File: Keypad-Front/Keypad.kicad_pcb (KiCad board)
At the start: 4 copper layers, 100.1 x 192.1 mm, 62 parts, among them J1 RTC STEMMA QT, J3 JST-PH 6, J4 JST-PH 6, J6 EXP QWIIC, J7 TOUCH QWIIC, U1 DS3231MZ, U2 LM1117-3.3, U3 CAP1214

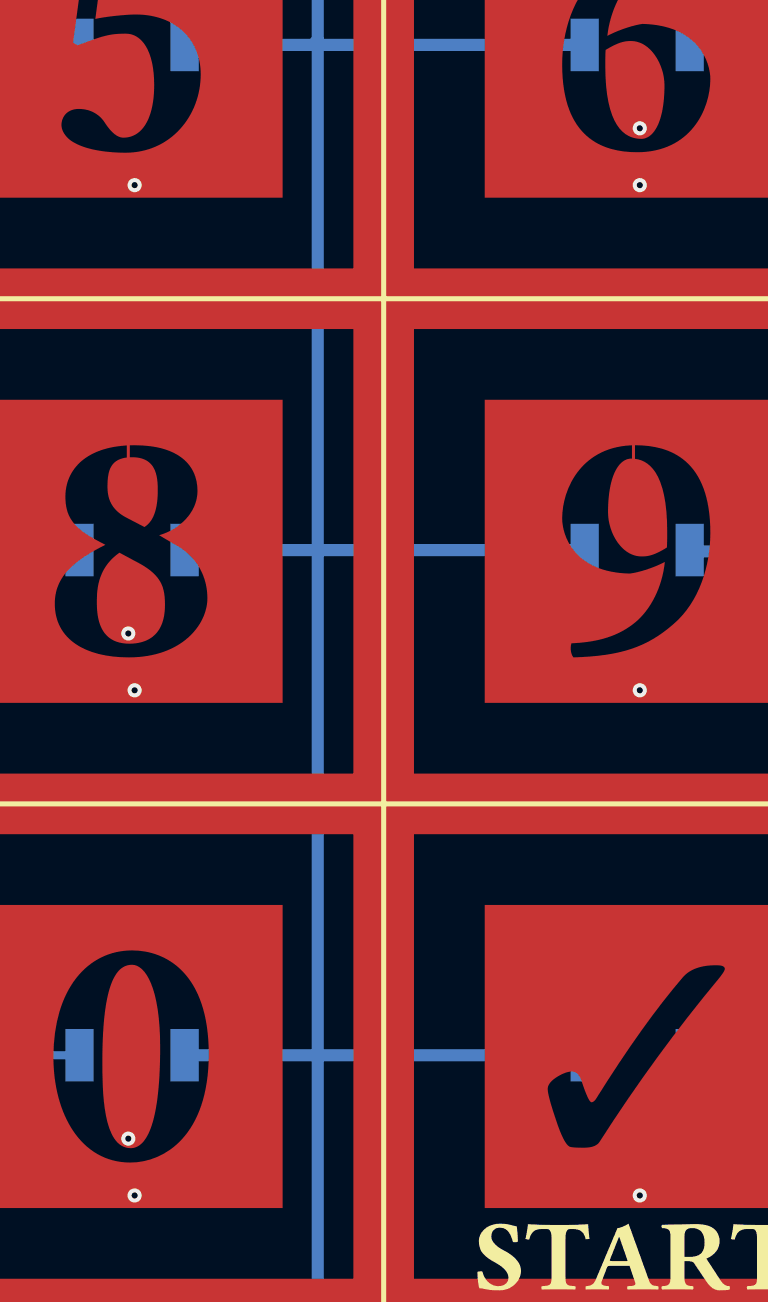
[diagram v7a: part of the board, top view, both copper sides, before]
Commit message: Third version, no vias to cast shadows.
Also add the BOM.
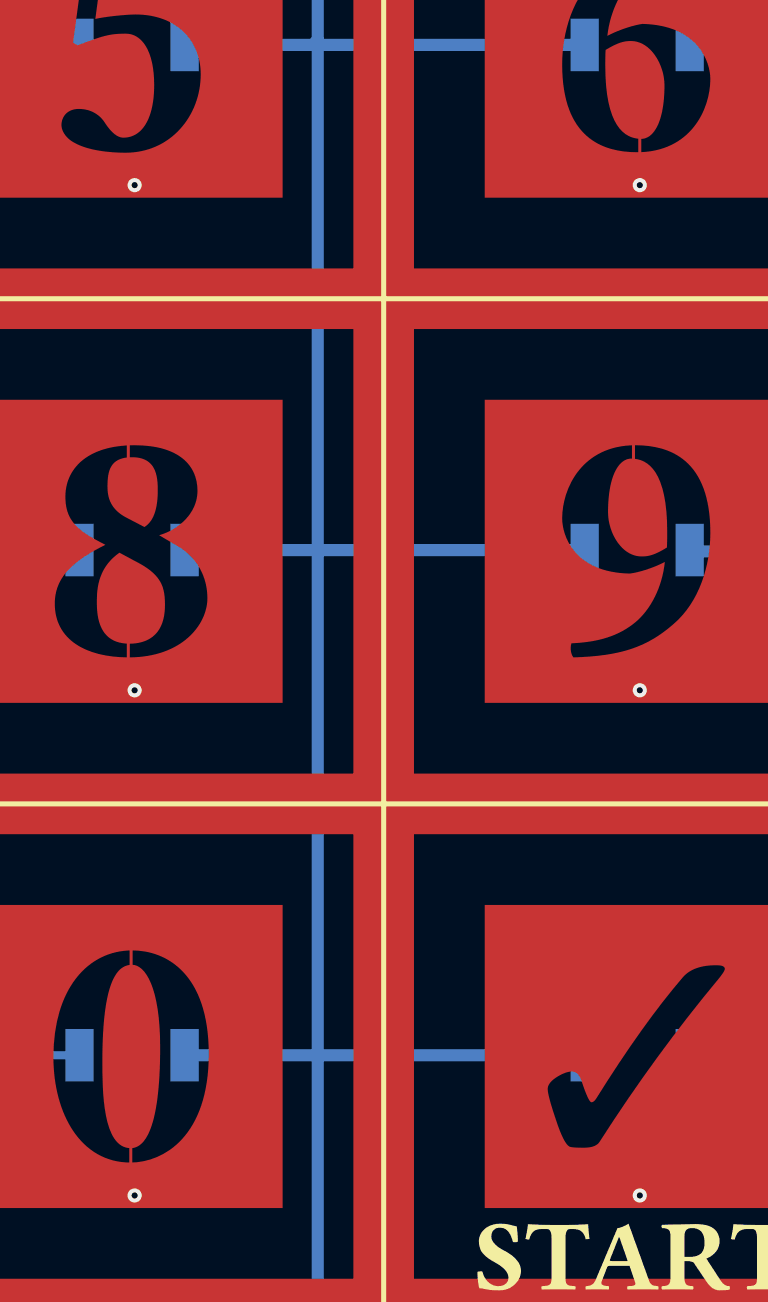
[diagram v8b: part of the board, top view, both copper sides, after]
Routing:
- net /TOUCH_11: track 22.0 -> 24.0 mm, vias 3 -> 2
- net /TOUCH_8: track 50.8 -> 50.4 mm, vias 3 -> 2
- net /TOUCH_6: vias 3 -> 2
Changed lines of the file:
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@@
   (segment (start 107.285311 184.267544) (end 106.5625 183.544733) (width 0.15) (layer "B.Cu") (net 48))
   (segment (start 106.5625 183.544733) (end 106.5625 181.875) (width 0.15) (layer "B.Cu") (net 48))
+  (segment (start 133.125 119.0625) (end 133.125 116.25) (width 0.15) (layer "F.Cu") (net 49))
   (segment locked (start 133.125 119.0625) (end 131.601 119.0625) (width 0.15) (layer "F.Cu") (net 49))
   (via (at 113.4375 181.875) (size 0.7) (drill 0.3) (layers "F.Cu" "B.Cu") (net 49))
-  (via (at 133.125 116.25) (size 0.7) (drill 0.3) (layers "F.Cu" "B.Cu") (net 49))
   (via locked (at 133.125 119.0625) (size 0.7) (drill 0.3) (layers "F.Cu" "B.Cu") (net 49))
   (segment (start 142.1875 127.8125) (end 142.1875 148.4375) (width 0.15) (layer "In1.Cu") (net 49))
@@
   (segment (start 133.125 119.0625) (end 133.4375 119.0625) (width 0.15) (layer "In1.Cu") (net 49))
   (segment (start 115.9375 179.6875) (end 115.625 179.6875) (width 0.15) (layer "In1.Cu") (net 49))
-  (segment (start 133.125 119.0625) (end 133.125 116.25) (width 0.15) (layer "In1.Cu") (net 49))
   (segment (start 133.4375 119.0625) (end 142.1875 127.8125) (width 0.15) (layer "In1.Cu") (net 49))
   (segment (start 115.625 179.6875) (end 113.4375 181.875) (width 0.15) (layer "In1.Cu") (net 49))
@@
   (segment (start 103.75 182.853553) (end 103.75 181.875) (width 0.15) (layer "B.Cu") (net 50))
   (segment (start 106.224651 185.328204) (end 103.75 182.853553) (width 0.15) (layer "B.Cu") (net 50))
+  (segment (start 107.8125 143.75) (end 107.8125 141.25) (width 0.15) (layer "F.Cu") (net 51))
   (segment locked (start 108.125 144.0625) (end 106.601 144.0625) (width 0.15) (layer "F.Cu") (net 51))
   (via (at 107.5 181.875) (size 0.7) (drill 0.3) (layers "F.Cu" "B.Cu") (net 51))
   (via locked (at 108.125 144.0625) (size 0.7) (drill 0.3) (layers "F.Cu" "B.Cu") (net 51))
-  (via (at 107.8125 141.25) (size 0.7) (drill 0.3) (layers "F.Cu" "B.Cu") (net 51))
   (segment (start 107.5 180) (end 107.5 181.875) (width 0.15) (layer "In1.Cu") (net 51))
-  (segment (start 108.125 144.0625) (end 107.8125 143.75) (width 0.15) (layer "In1.Cu") (net 51))
   (segment (start 100.3125 169.6875) (end 105 174.375) (width 0.15) (layer "In1.Cu") (net 51))
   (segment (start 105 177.5) (end 107.5 180) (width 0.15) (layer "In1.Cu") (net 51))
-  (segment (start 107.8125 143.75) (end 107.8125 141.25) (width 0.15) (layer "In1.Cu") (net 51))
   (segment (start 100.3125 151.875) (end 100.3125 169.6875) (width 0.15) (layer "In1.Cu") (net 51))
   (segment (start 105 174.375) (end 105 177.5) (width 0.15) (layer "In1.Cu") (net 51))
@@
   (segment (start 104.6875 183.083947) (end 104.6875 181.875) (width 0.15) (layer "B.Cu") (net 53))
   (segment (start 106.578204 184.974651) (end 104.6875 183.083947) (width 0.15) (layer "B.Cu") (net 53))
+  (segment (start 107.934694 168.254966) (end 107.934694 165.754966) (width 0.15) (layer "F.Cu") (net 54))
   (segment locked (start 108.125 169.0625) (end 106.601 169.0625) (width 0.15) (layer "F.Cu") (net 54))
-  (via (at 107.8125 166.25) (size 0.7) (drill 0.3) (layers "F.Cu" "B.Cu") (net 54))
+  (segment (start 107.951146 158.614251) (end 107.951146 156.114251) (width 0.15) (layer "F.Cu") (net 54))
   (via (at 108.75 181.875) (size 0.7) (drill 0.3) (layers "F.Cu" "B.Cu") (net 54))
   (via locked (at 108.125 169.0625) (size 0.7) (drill 0.3) (layers "F.Cu" "B.Cu") (net 54))
-  (segment (start 107.8125 168.75) (end 107.8125 166.25) (width 0.15) (layer "In1.Cu") (net 54))
   (segment (start 111.25 172.1875) (end 108.125 169.0625) (width 0.15) (layer "In1.Cu") (net 54))
-  (segment (start 108.125 169.0625) (end 107.8125 168.75) (width 0.15) (layer "In1.Cu") (net 54))
   (segment (start 111.25 176.5625) (end 111.25 172.1875) (width 0.15) (layer "In1.Cu") (net 54))
   (segment (start 108.75 181.875) (end 108.75 179.0625) (width 0.15) (layer "In1.Cu") (net 54))
